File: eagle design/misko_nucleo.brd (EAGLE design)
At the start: 115 x 115 mm, 135 parts, among them IC1 ATMEGA1281-16AU, IC10 ORG1510-MK4, IC11 TPS3808G33DBVT, IC12 LTC4425, IC13 RN4678_BT_MODULE, IC14 ADXL345, IC15 74HCT1G32, IC16 FM25W256-SOIC, IC17 MICROSD_SPI_MODE, IC18 FH12-30S-0.5SH, IC19 DS1394U-33+, IC2 MC1525TT, IC23 SP3012-04UTG, IC3 TMP36GRTZ, IC4 TPS63031, IC5 MCP73871-2AAI/ML, IC6 MAX6818, IC7 FT230XS, IC8 SN74LVC1G3157DBVR - BT switch, IC9 SN74LVC1G3157DBVR - GPS switch, Q1 ABM3B-8MHZ-10-1-U-T, Q2 LFXTAL016178R, SW1 RESET, SW2 POWER SWITCH, SW3 MICROJOYSTICK, SW4 PB6156RSL, SW5 PB6156RSL, T1 BSS84

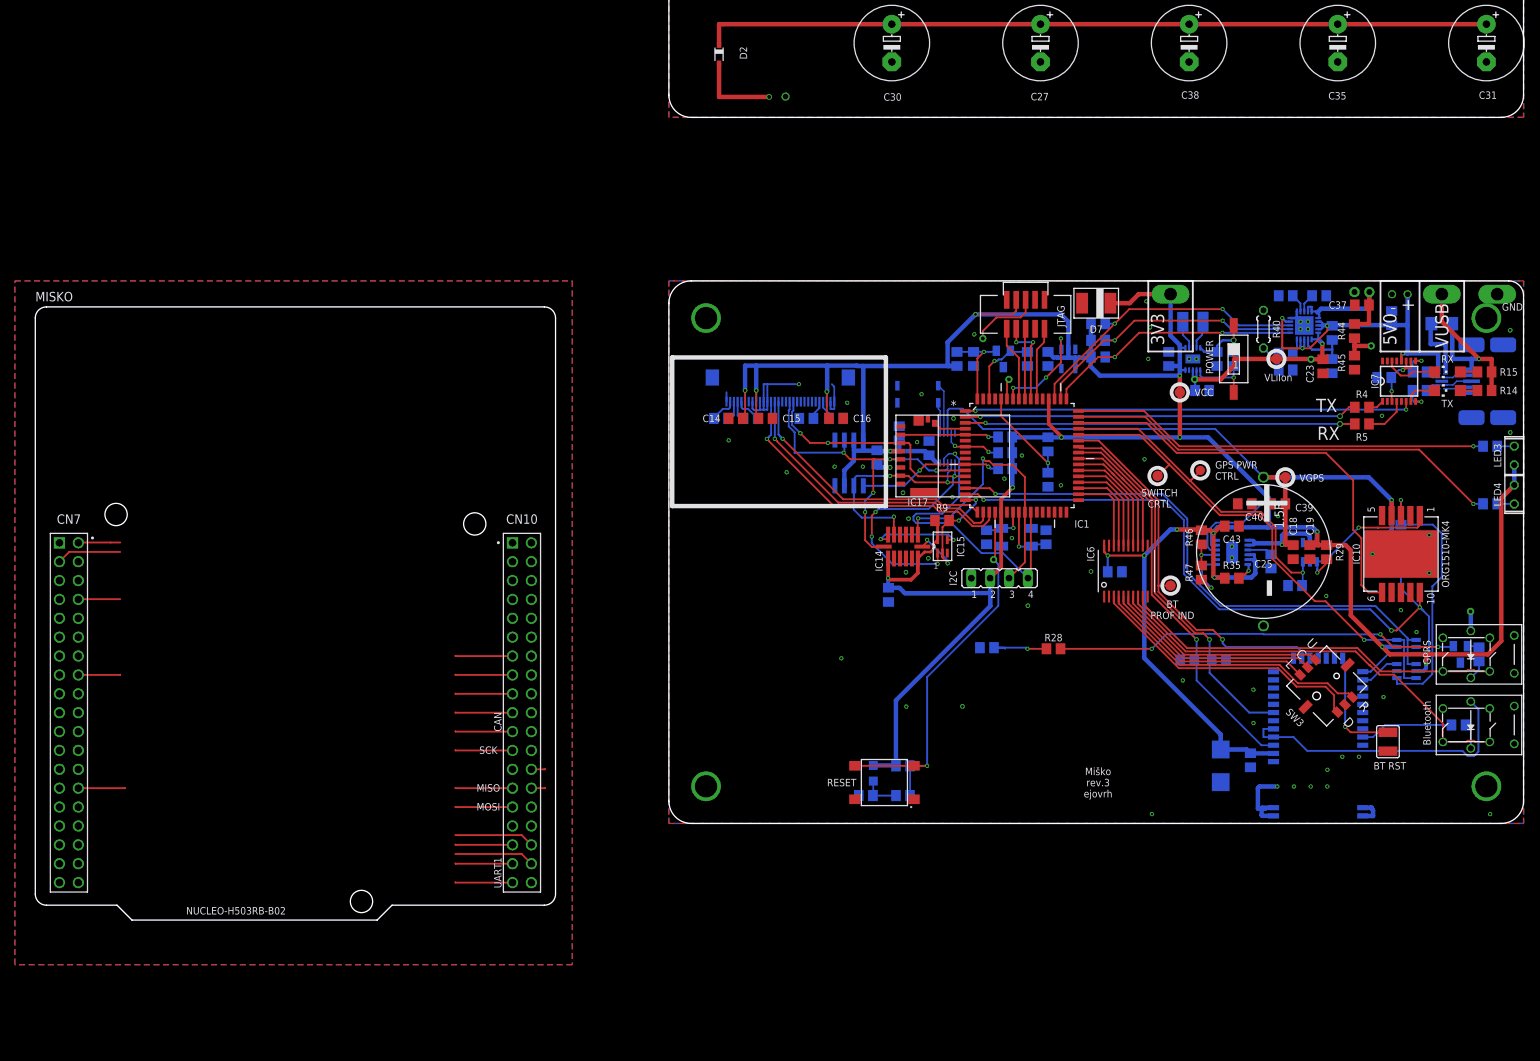
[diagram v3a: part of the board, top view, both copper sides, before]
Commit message: - added ADXL345 module to schematic
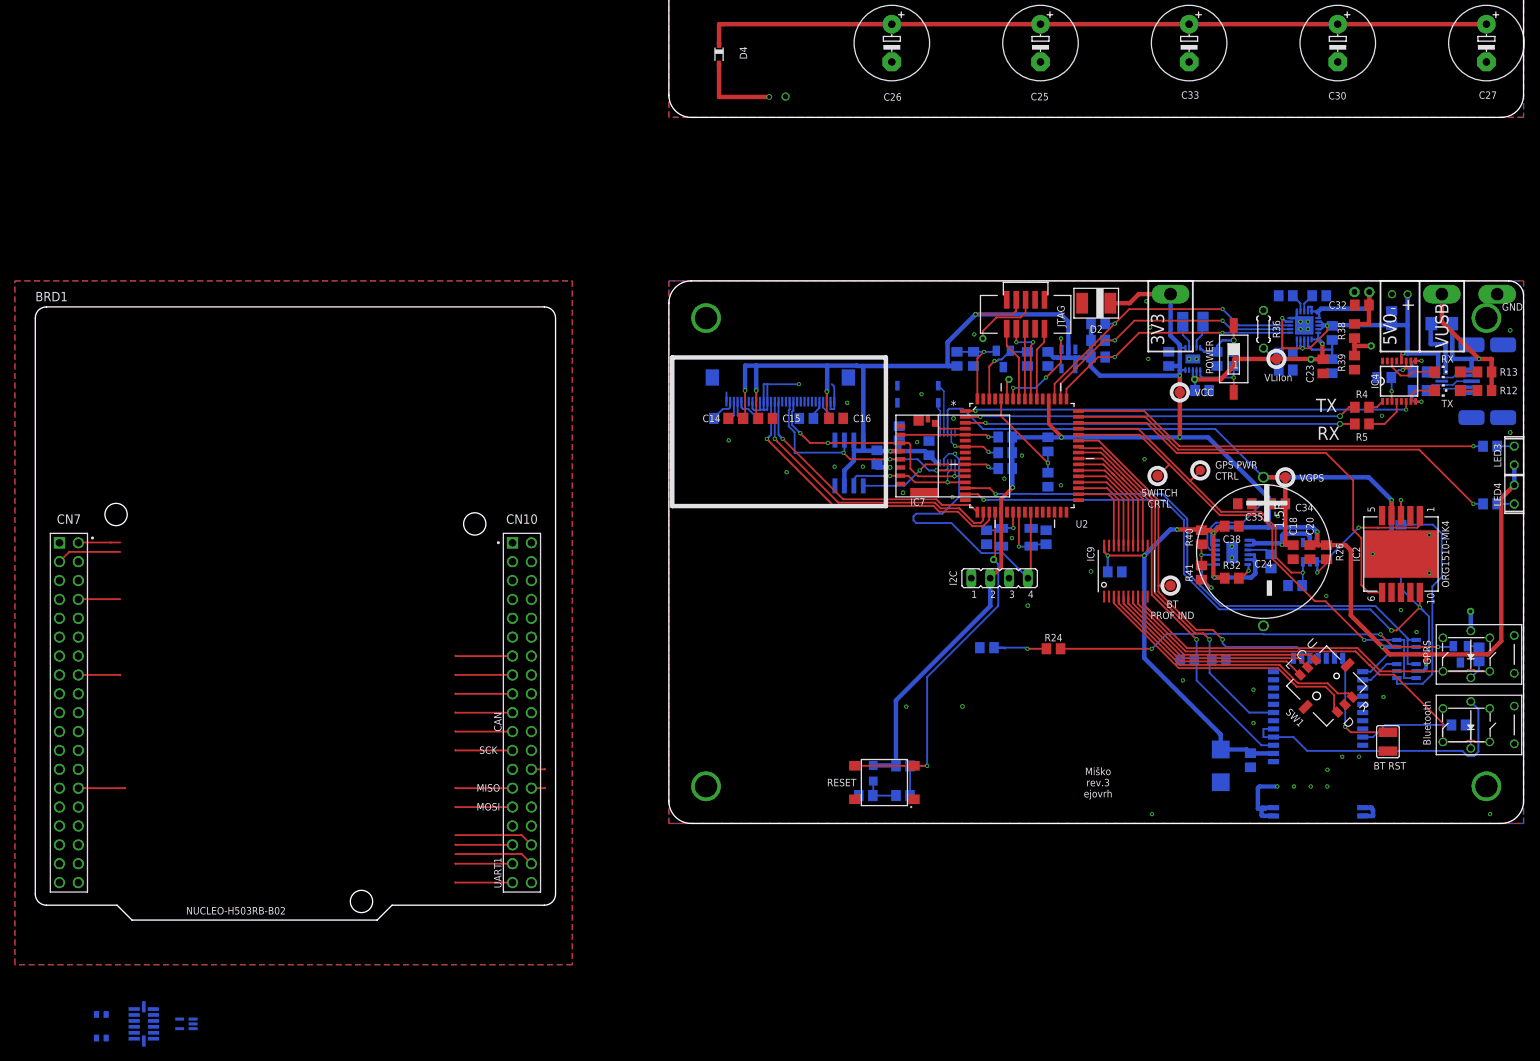
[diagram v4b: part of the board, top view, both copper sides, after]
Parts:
- removed C39, C40: 100µF, rcl:C0805
- removed C41, C42: 0.1µF, resistor:C0805
- removed C43, C45: 0.1µF, rcl:C0805
- removed CONN4: USB mini B, MX-67503-1230 USB Mini-B SMT straight socket:SMT
- removed D7: BZG05C3V6-E3-TR3, zener:DO-214
- removed IC12: LTC4425, LTC4425 Supercap Charger:MSOP
- removed IC13: RN4678_BT_MODULE, RN4678 Bluetooth 4.2 Dual Mode:SMT
- removed IC14: ADXL345, ADXL345 Accelerometer:LGA14
- removed IC15: 74HCT1G32, 74HCT1G32GW:SOT353/5
- removed IC16: FM25W256-SOIC, FM25W256 FERAM:SOIC08
- removed IC17: MICROSD_SPI_MODE, Molex SD-47309 SD Card Slot:MICRO_SD_CONNECTOR
- removed IC19: DS1394U-33+, DS1394U-33+ RTC SPI Module:10UMAX
- removed IC23: SP3012-04UTG, SP3012 TVS Diode Array:μDFN-10
- removed R42, R43: 10k, resistor:R0805
- removed R45: 150k, rcl:R0805
- removed R46, R47: 470k, resistor:R0805
- removed SW4, SW5: PB6156RSL, PB6156RSL Illuminated Tact SPST-NO switch:TH
- removed T1: BSS84, transistor-small-signal:SOT23
- added C104: 0.1u / 16V, rcl:C0402
- added C22, C28: 0.1µF, rcl:C0805
- added C24: 1.5F, EECS5R5H155 Supercap:TH
- added C26, C33: 1000µF, rcl:E5-10,5
- added D3: SZ1SMB5916BT3G, diode:SMB
- added IC101: ADXL345, ADXL345 Accelerometer:LGA14
- added IC102: 74HCT1G32GW, 74HCT1G32GW - OR Gate:SOT353/5
- added JP1: I2C, jumper:JP4
- added Q3: LFXTAL016178R, LFXTAL016178R 32.768kHz crystal:SMD
- added R101: 10k, rcl:R0402
- added R11: 270k, rcl:R0805
- added R21: 47k, rcl:R0805
- added R24: 10k, resistor:R0805
- added R31: 1k, rcl:R0805
- added S1: RESET, Wurth_Elektronik_Electromechanic_Switch_rev17c:430152050836
- added S2: POWER SWITCH, smd-special:SMS-001
- added U1: SN74LVC1G3157DBVR - BT switch, Texas Instruments_By_element14_Batch_1:SOT95P280X145-6N
- added U2: ATMEGA1281-16AU, Atmel_By_element14_Batch_1-00:QFP80P1600X1600X120-64N
- added U3: TPS3808G33DBVT, Texas Instruments_By_element14_Batch_1:SOT95P280X145-6N
- added U4: TMP36GRTZ, TMP36GRTZ:SOT95P280X145-5N
- added U5: MCP73871-2AAI/ML, MCP73871 - Powerpath and Charge Controller:QFN50P400X400X100-21N
- added U6: SN74LVC1G3157DBVR - GPS switch, Texas Instruments_By_element14_Batch_1:SOT95P280X145-6N
- C19: value 0.1µF -> 10µF
- C20, C5: device resistor:C0805 -> rcl:C0805
- C21, C36: device rcl:C0805 -> resistor:C0805
- C25: value 1.5F -> 1000µF; device EECS5R5H155 Supercap:TH -> rcl:E5-10,5
- C31, C38: value 1000µF -> 0.1µF; device rcl:E5-10,5 -> rcl:C0805
- C32, C4: value 0.1µF -> 10µF; device rcl:C0805 -> resistor:C0805
- C34: value 10µF -> 100µF
- C35: value 1000µF -> 100µF; device rcl:E5-10,5 -> rcl:C0805
- C37, C6: value 10µF -> 0.1µF
- CONN1: value JTAG -> USB mini B; device JTAG 1.27mm 10pin header:TH-JTAG -> MX-67503-1230 USB Mini-B SMT straight socket:SMT
- CONN2: value I2C -> JTAG; device jumper:JP4 -> JTAG 1.27mm 10pin header:TH-JTAG
- D2: value BAT60AE6327 -> BZG05C3V6-E3-TR3; device diode:SOD323_ST -> zener:DO-214
- D4: value SZ1SMB5916BT3G -> BAT60AE6327; device diode:SMB -> diode:SOD323_ST
- IC1: value ATMEGA1281-16AU -> MC1525TT; device Atmel_By_element14_Batch_1-00:QFP80P1600X1600X120-64N -> microchip:SOT23
- IC10: value ORG1510-MK4 -> LTC4425; device ORG1510-MK4 GPS module:PACKAGE -> LTC4425 Supercap Charger:MSOP
- IC11: value TPS3808G33DBVT -> SP3012-04UTG; device Texas Instruments_By_element14_Batch_1:SOT95P280X145-6N -> SP3012 TVS Diode Array:μDFN-10
- IC2: value MC1525TT -> ORG1510-MK4; device microchip:SOT23 -> ORG1510-MK4 GPS module:PACKAGE
- IC3: value TMP36GRTZ -> TPS63031; device TMP36GRTZ:SOT95P280X145-5N -> TPS63031 - Buck Boost Voltage Regulator:SMT
- IC4: value TPS63031 -> FT230XS; device TPS63031 - Buck Boost Voltage Regulator:SMT -> ftdichip:SSOP16
- IC5: value MCP73871-2AAI/ML -> RN4678_BT_MODULE; device MCP73871 - Powerpath and Charge Controller:QFN50P400X400X100-21N -> RN4678 Bluetooth 4.2 Dual Mode:SMT
- IC6: value MAX6818 -> FM25W256-SOIC; device MAX6818 CMOS Switch debouncer:TSSOP20 -> FM25W256 FERAM:SOIC08
- IC7: value FT230XS -> MICROSD_SPI_MODE; device ftdichip:SSOP16 -> Molex SD-47309 SD Card Slot:MICRO_SD_CONNECTOR
- IC8: value SN74LVC1G3157DBVR - BT switch -> DS1394U-33+; device Texas Instruments_By_element14_Batch_1:SOT95P280X145-6N -> DS1394U-33+ RTC SPI Module:10UMAX
- IC9: value SN74LVC1G3157DBVR - GPS switch -> MAX6818; device Texas Instruments_By_element14_Batch_1:SOT95P280X145-6N -> MAX6818 CMOS Switch debouncer:TSSOP20
- L1: value DL0805-33 33µH -> DJNR3015-1R5; device rcl:L0805 -> DJNR3015-1R5 Inductor:FFF
- L2: value DJNR3015-1R5 -> DL0805-33 33µH; device DJNR3015-1R5 Inductor:FFF -> rcl:L0805
- Q2: value LFXTAL016178R -> BSS84; device LFXTAL016178R 32.768kHz crystal:SMD -> transistor-small-signal:SOT23
- R10: value 27 -> 100k; device resistor:R0805 -> rcl:R0805
- R12: value 100k -> 1k; device rcl:R0805 -> resistor:R0805
- R13: value 270k -> 1k; device rcl:R0805 -> resistor:R0805
- R14, R18: value 1k -> 10k
- R15: value 1k -> 47k; device resistor:R0805 -> rcl:R0805
- R16: value 47k -> 1k
- R19: value 10k -> 47k
- R20, R25: value 47k -> 1k; device rcl:R0805 -> resistor:R0805
- R22: value 1k -> 390k; device resistor:R0805 -> rcl:R0805
- R26: value 390k -> 1M; device rcl:R0805 -> resistor:R0805
- R29: value 1M -> 10k; device resistor:R0805 -> rcl:R0805
- R30: device resistor:R0805 -> rcl:R0805
- R32: value 10k -> 1k; device rcl:R0805 -> resistor:R0805
- R33: value 1k -> 10k; device rcl:R0805 -> resistor:R0805
- R34: value 1k -> 100k
- R35: value 1k -> 270k; device resistor:R0805 -> rcl:R0805
- R36: value 10k -> NTC 10k; device resistor:R0805 -> rcl:0204/5
- R37: value 100k -> 10k
- R39: value 270k -> 150k
- R40: value NTC 10k -> 470k; device rcl:0204/5 -> resistor:R0805
- R41: value 10k -> 470k; device rcl:R0805 -> resistor:R0805
- R9: value 10k -> 27; device rcl:R0805 -> resistor:R0805
- SW1: value RESET -> MICROJOYSTICK; device Wurth_Elektronik_Electromechanic_Switch_rev17c:430152050836 -> micro joystick:MICROJOYSTICK
- SW2: value POWER SWITCH -> PB6156RSL; device smd-special:SMS-001 -> PB6156RSL Illuminated Tact SPST-NO switch:TH
- SW3: value MICROJOYSTICK -> PB6156RSL; device micro joystick:MICROJOYSTICK -> PB6156RSL Illuminated Tact SPST-NO switch:TH
- moved D4 117.1 mm to (92.0, 116.5), flipped to the top
- moved R22 97.0 mm to (103.8, 67.5)
- moved C31 94.9 mm to (116.2, 65.5), flipped to the bottom, turned to 90 degrees
- moved Q2 81.0 mm to (191.8, 35.8), turned to 180 degrees
- moved C25 74.6 mm to (135.2, 118.0), turned to 270 degrees
- moved R26 72.3 mm to (173.8, 49.5), flipped to the top, turned to 90 degrees
- moved R20 70.9 mm to (191.5, 26.2)
- moved IC7 69.5 mm to (115.8, 56.9)
- moved R25 67.9 mm to (194.2, 35.8), turned to 90 degrees
- moved IC8 67.3 mm to (122.8, 63.5), turned to 270 degrees
- moved R9 67.3 mm to (186.2, 73.8), flipped to the bottom, turned to 180 degrees
- moved R18 65.4 mm to (130.5, 60.8)
- moved C38 65.3 mm to (161.0, 53.0), turned to 180 degrees
- moved C35 63.2 mm to (162.8, 56.0), turned to 0 degrees
- moved C32 61.3 mm to (178.5, 82.8), flipped to the top, turned to 180 degrees
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- renumbered CONN3 to CN1, IC18 to X1, MISKO to BRD1, R44 to R38, SJ3 to SJ1
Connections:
- removed net ADXL345SDA: IC14.SDA, IC15.Y
- removed net ADXL345_INT: BRD1.CN10_17
- new net ADXL345:ADXL345SDA: IC101.SDA, IC102.Y
- new net ADXL345:ADXL345_INT2: IC101.INT2
- new net ADXL345_INT1: BRD1.CN10_17, IC101.INT1
- net 3V3: now also C104.1, IC101.VCC, IC101.VDD, IC102.VCC, R101.2
- net ADXL345_CS: now also IC101.!CS!, IC102.A, R101.1
- net ADXL345_INT1_INTERRUPT_PIN: now also JP1.3, U2.25; no longer CONN2.3, IC1.25, IC14.INT1
- net ANALOG_SW_CTRL_PIN: now also U1.6, U2.44, U6.6; no longer IC1.44, IC8.6, IC9.6
- net AREF: now also C4.1, IC1.2, U2.62; no longer C5.1, IC1.62, IC2.2
- net AVCC: now also C36.2, IC1.1, L2.2, U2.64; no longer C41.2, IC1.64, IC2.1, L1.2
- net BAT_A_PIN: now also R39.1, U2.59; no longer IC1.59, R45.1
- net BLUETOOTH_PROF_IND_PIN: now also IC5.P0_5, U2.43; no longer IC1.43, IC13.P0_5
- net BLUETOOTH_RX: now also IC5.RXD, U1.4; no longer IC13.RXD, IC8.4
- net BLUETOOTH_SWITCH_PIN: now also IC5.SW_BTN, R28.2, U2.41; no longer IC1.41, IC13.SW_BTN, R43.2
- net BLUETOOTH_TX: now also IC5.TXD, U6.3; no longer IC13.TXD, IC9.3
- net BLUETOOTH_WAKEUP_PIN: now also IC5.WAKEUP, R27.2, U2.42; no longer IC1.42, IC13.WAKEUP, R42.2
- net BT_LED: now also IC5.LED, R20.1; no longer IC13.LED, R22.1
- net BUTTON_BLUETOOTH: now also IC9.IN7, SW3.3, SW3.4; no longer IC6.IN7, SW4.3, SW4.4
- net BUTTON_CENTER: now also IC9.IN5, SW1.CENTER; no longer IC6.IN5, SW3.CENTER
- net BUTTON_DOWN: now also IC9.IN2, SW1.DOWN; no longer IC6.IN2, SW3.DOWN
- net BUTTON_GPRS: now also IC9.IN8, SW2.3, SW2.4; no longer IC6.IN8, SW5.3, SW5.4
- net BUTTON_LEFT: now also IC9.IN4, SW1.LEFT; no longer IC6.IN4, SW3.LEFT
- net BUTTON_RIGHT: now also IC9.IN3, SW1.RIGHT; no longer IC6.IN3, SW3.RIGHT
- net BUTTON_UP: now also IC9.IN6, SW1.UP; no longer IC6.IN6, SW3.UP
- net CBUS1: now also IC4.14; no longer IC7.14
- net CBUS2: now also IC4.7; no longer IC7.7
- net D+: now also CONN1.D+, IC11.4; no longer CONN4.D+, IC23.4
- net D-: now also CONN1.D-, IC11.2; no longer CONN4.D-, IC23.2
- net EN: now also IC3.6_EN, S2.1; no longer IC4.6_EN, SW2.1
- net GND: now also C104.2, C19.2, C20.1, C22.2, C24.-, C26.-, C28.2, C31.2, C33.-, C35.1, C36.1, C37.1, C38.1, C5.1, C6.2, CONN1.GND1, CONN1.GND2, CONN1.GND3, CONN1.GND4, CONN1.GND5, CONN2.10_GND, CONN2.2_GND, D2.AN, D3.A, IC1.3, IC101.GND1, IC101.GND2, IC101.GND3, IC102.GND, IC11.3, IC2.GND1, IC2.GND2, IC2.GND3, IC2.GND4, IC2.GND5, IC3.3_PGND, IC3.9_GND1, IC3.GND2, IC3.GND3, IC3.GND4, IC4.13, IC4.5, IC5.GND, IC5.GND1, IC5.GND10, IC5.GND11, IC5.GND12, IC5.GND7, IC5.GND8, IC5.GND9, IC7.GND2, IC7.GND4, IC7.POL, IC7.VSS, IC8.GND, IC9.!EN!, IC9.GND, JP1.1, Q2.3, R11.2, R14.2, R22.1, R27.1, R28.1, R31.2, R33.1, R35.2, R36.2, S1.1, S1.3, SW1.GND1, SW1.GND2, SW1.GND3, SW2.1, SW2.2, SW2.GND1, SW2.GND2, SW3.1, SW3.2, U1.2, U2.22, U2.53, U2.63, U3.2, U4.5, U5.10_GND1, U5.11_GND2, U5.GND2, U5.GND3, U5.GND4, U5.GND5, U5.GND6, U6.2; no longer C19.1, C20.2, C31.-, C34.2, C35.-, C36.2, C37.2, C38.-, C40.1, C41.1, C42.1, C43.1, C45.2, C5.2, C6.1, CONN1.10_GND, CONN1.2_GND, CONN2.1, CONN4.GND1, CONN4.GND2, CONN4.GND3, CONN4.GND4, CONN4.GND5, D4.A, D7.AN, IC1.22, IC1.53, IC1.63, IC10.GND4, IC10.GND5, IC11.2, IC12.GND1, IC12.GND2, IC12.GND3, IC13.GND, IC13.GND1, IC13.GND10, IC13.GND11, IC13.GND12, IC13.GND2, IC13.GND3, IC13.GND4, IC13.GND5, IC13.GND6, IC13.GND7, IC13.GND8, IC13.GND9, IC14.GND1, IC14.GND2, IC14.GND3, IC15.GND, IC16.GND, IC17.GND2, IC17.GND4, IC17.POL, IC17.VSS, IC19.GND, IC2.3, IC23.3, IC3.5, IC4.3_PGND, IC4.9_GND1, IC4.GND2, IC4.GND3, IC4.GND4, IC5.10_GND1, IC5.11_GND2, IC6.!EN!, IC7.13, IC7.5, IC8.2, IC9.2, R13.2, R26.1, R27.2, R36.1, R37.2, R40.2, R42.1, R43.1, R45.2, SW1.1, SW1.3, SW3.GND3, SW4.1, SW4.2, SW4.GND1, SW4.GND2, SW5.1, SW5.2, SW5.GND1, SW5.GND2, T1.3
- net GPRS_NETLIGHT: now also R23.1, R24.1; no longer R27.1, R28.1
- net GPRS_NETLIGHT_GATE: now also Q2.1, R24.2; no longer R28.2, T1.1
- net GPS_GREEN_LED_PIN: now also R16.1, U2.48; no longer IC1.48, R17.1
- net GPS_ON_OFF: now also IC2.ON_OFF, R26.1, U3.1; no longer IC10.ON_OFF, IC11.1, R29.1
- net GPS_POWER_CTL_PIN: now also R14.1, U2.45, U3.3; no longer IC1.45, IC11.3, R23.1
- net GPS_RED_LED_PIN: now also R17.1, U2.47; no longer IC1.47, R18.1
- net GPS_SW_SERIAL_RX: now also U1.1, U2.14, U6.4; no longer IC1.14, IC8.1, IC9.4
- net GPS_SW_SERIAL_TX: now also IC2.RX, U1.3, U2.15; no longer IC1.15, IC10.RX, IC8.3
- net GPS_TX: now also IC2.TX, U6.1; no longer IC10.TX, IC9.1
- net GPS_WAKEUP_PIN: now also IC2.WAKEUP, U2.46; no longer IC1.46, IC10.WAKEUP
- net GREEN_LED: now also R16.2; no longer R17.2
- net ID: now also CONN1.ID, IC11.5; no longer CONN4.ID, IC23.5
- net IREF: now also R22.2; no longer R26.2
- net JTAG_TCL_PIN: now also CONN2.1_JTAG_TCK, U2.57; no longer CONN1.1_JTAG_TCK, IC1.57
- net JTAG_TDI_PIN: now also CONN2.9_JTAG_TDI, U2.54; no longer CONN1.9_JTAG_TDI, IC1.54
- net JTAG_TDO_PIN: now also CONN2.3_JTAG_TDO, U2.55; no longer CONN1.3_JTAG_TDO, IC1.55
- net JTAG_TMS_PIN: now also CONN2.5_JTAG_TMS, U2.56; no longer CONN1.5_JTAG_TMS, IC1.56
- net L2: now also R20.2, SW3.L2; no longer R22.2, SW4.L2
- net LDO18_O: now also IC5.LDO18_O; no longer IC13.LDO18_O
- net LDO33_O: now also IC5.LDO33_O, IC5.VDD_IO, SW3.L1; no longer IC13.LDO33_O, IC13.VDD_IO, SW4.L1
- net LTC4425_EN: now also IC10.EN, R32.2; no longer IC12.EN, R35.2
- net LTC4425_PROG: now also IC10.PROG, R33.2; no longer IC12.PROG, R36.2
- net L_L1: now also IC3.4_L1, L1.P$1; no longer IC4.4_L1, L2.P$1
- net L_L2: now also IC3.2_L2, L1.P$2; no longer IC4.2_L2, L2.P$2
- net MCP73871_CHARGE_STATUS_1_PIN: now also R21.2, U2.51, U5.8_STAT1; no longer IC1.51, IC5.8_STAT1, R25.2
- net MCP73871_CHARGE_STATUS_2_PIN: now also R19.2, U2.50, U5.7_STAT2; no longer IC1.50, IC5.7_STAT2, R20.2
- net MCP73871_POWER_GOOD_PIN: now also R15.2, U2.49, U5.!6_PG!; no longer IC1.49, IC5.!6_PG!, R16.2
- net MENU_BLUETOOTH_POWER_BUTTON_PIN: now also IC9.OUT7, U2.39; no longer IC1.39, IC6.OUT7
- net MENU_CENTER_BUTTON_PIN: now also IC9.OUT5, U2.37; no longer IC1.37, IC6.OUT5
- net MENU_DOWN_BUTTON_PIN: now also IC9.OUT2, U2.34; no longer IC1.34, IC6.OUT2
- net MENU_GPRS_POWER_BUTTON_PIN: now also IC9.OUT8, U2.40; no longer IC1.40, IC6.OUT8
- net MENU_LEFT_BUTTON_PIN: now also IC9.OUT4, U2.36; no longer IC1.36, IC6.OUT4
- net MENU_RIGHT_BUTTON_PIN: now also IC9.OUT3, U2.35; no longer IC1.35, IC6.OUT3
- net MENU_UP_BUTTON_PIN: now also IC9.OUT6, U2.38; no longer IC1.38, IC6.OUT6
- net N$1: now also R25.1, SW2.L2; no longer R30.1, SW5.L2
- net N$10: now also IC4.10, IC4.11, IC4.3; no longer IC7.10, IC7.11, IC7.3
- net N$11: now also IC5.!RST_N!; no longer IC13.!RST_N!
- net N$19: now also R30.2, R35.1, R36.1; no longer R33.2, R39.1, R40.1
- net N$3: now also Q2.2, R25.2; no longer R30.2, T1.2
- net N$4: now also IC11.1; no longer IC23.1
- net N$6: now also C25.+, C26.+, C33.+, D4.C; no longer C31.+, C35.+, C38.+, D2.C
- net OLD_5V0: now also C37.2, D4.A, IC11.10, IC4.12, R10.1, U5.17_CE, U5.18_IN1, U5.19_IN2, U5.3_SEL, U5.4_PROG2, U5.9_!TE!; no longer C42.2, D2.A, IC23.10, IC5.17_CE, IC5.18_IN1, IC5.19_IN2, IC5.3_SEL, IC5.4_PROG2, IC5.9_!TE!, IC7.12, R12.1
- net PDI_UART0_CTS_PIN: now also IC4.6, U2.1; no longer IC1.1, IC7.6
- net PDI_UART0_RX_PIN: now also U2.2; no longer IC1.2
- net PDI_UART0_TX_PIN: now also U2.3; no longer IC1.3
- net PFI: now also IC10.PFI, R40.1, R41.2; no longer IC12.PFI, R46.1, R47.2
- net PFI_RET: now also IC10.PFI_RET, R41.1; no longer IC12.PFI_RET, R47.1
- net PROG1: now also R31.1, U5.13_PROG1; no longer IC5.13_PROG1, R34.1
- net PROG3: now also R34.1, U5.12_PROG3; no longer IC5.12_PROG3, R37.1
- net RED_LED: now also R17.2; no longer R18.2
- net RESET: now also CONN2.6_JTAG_RST, S1.2, S1.4, U2.20; no longer CONN1.6_JTAG_RST, IC1.20, SW1.2, SW1.4
- net RTC_INT_INTERRUPT_PIN: now also IC8.!INT!, JP1.4, U2.26; no longer CONN2.4, IC1.26, IC19.!INT!
- net RTC_XTAL1: now also IC8.X1, Q3.XTAL1; no longer IC19.X1, Q2.XTAL1
- net RTC_XTAL2: now also IC8.X2, Q3.XTAL2; no longer IC19.X2, Q2.XTAL2
- net RXD: now also IC4.4; no longer IC7.4
- net SD_CARD_DETECT_PIN: now also IC7.DET, U2.4; no longer IC1.4, IC17.DET
- net SPI1_MISO: now also IC101.SDO
- net SPI1_MOSI: now also IC102.B
- net SPI1_SCK: now also IC101.SCL
- net SPI_MISO_PIN: now also IC6.SO, IC7.DAT0, IC8.DOUT, U2.13; no longer IC1.13, IC14.SDO, IC16.SO, IC17.DAT0, IC19.DOUT
- net SPI_MOSI_PIN: now also IC6.SI, IC7.CMD, IC8.DIN, U2.12; no longer IC1.12, IC15.B, IC16.SI, IC17.CMD, IC19.DIN
- net SPI_OLED_D/C_PIN: now also U2.17; no longer IC1.17
- net SPI_OLED_RESET_PIN: now also U2.18; no longer IC1.18
- net SPI_SCK_PIN: now also IC6.SCK, IC7.CLK, IC8.SCLK, U2.11; no longer IC1.11, IC14.SCL, IC16.SCK, IC17.CLK, IC19.SCLK
- net SPI_SS_ADXL345_PIN: now also U2.16; no longer IC1.16, IC14.!CS!, IC15.A, R9.2
- net SPI_SS_FRAM_PIN: now also IC6.!CS!, R18.1, U2.10; no longer IC1.10, IC16.!CS!, R19.1
- net SPI_SS_OLED_PIN: now also U2.19; no longer IC1.19
- net SPI_SS_RTC_PIN: now also IC8.!CS!, R29.2, U2.7; no longer IC1.7, IC19.!CS!, R32.2
- net SPI_SS_SD_CARD_PIN: now also IC7.CD/DAT3, R37.1, U2.5; no longer IC1.5, IC17.CD/DAT3, R41.1
- net THERM: now also R30.1, U5.5_THERM; no longer IC5.5_THERM, R33.1
- net TMP36_VSENSE_PIN: now also U2.58, U4.1; no longer IC1.58, IC3.1
- net TXD: now also IC4.1; no longer IC7.1
- net UART1_GPS_RX: now also U2.27; no longer IC1.27
- net UART1_GPS_TX: now also U2.28; no longer IC1.28
- net USBDM: now also IC4.9, R9.1; no longer IC7.9, R10.1
- net USBDP: now also IC4.8; no longer IC7.8
- net USB_D+: now also IC11.7; no longer IC23.7
- net USB_D-: now also IC11.9, R9.2; no longer IC23.9, R10.2
- net USB_ID: now also IC11.6; no longer IC23.6
- net USB_RX_LED: now also R12.2; no longer R14.2
- net USB_TX_LED: now also R13.2; no longer R15.2
- net VCC: now also C19.1, C20.2, C22.1, C28.1, C31.1, C38.2, CONN2.4_VCC, D2.CAT, D3.C, IC10.FB, IC10.SEL, IC10.VIN1, IC10.VIN2, IC3.10_FB, IC3.1_VOUT, IC5.BAT_IN, IC6.!HOLD!, IC6.!WP!, IC7.VDD, IC8.VCC, IC9.VCC, JP1.2, L2.1, R15.1, R18.2, R19.1, R21.1, R26.2, R29.1, R37.2, R40.2, U1.5, U2.21, U2.52, U3.6, U4.2, U4.4, U6.5; no longer C19.2, C20.1, C32.1, C34.1, C36.1, C4.1, C43.2, CONN1.4_VCC, CONN2.2, D4.C, D7.CAT, IC1.21, IC1.52, IC11.6, IC12.FB, IC12.SEL, IC12.VIN1, IC12.VIN2, IC13.BAT_IN, IC14.VCC, IC14.VDD, IC15.VCC, IC16.!HOLD!, IC16.!WP!, IC16.VCC, IC17.VDD, IC19.VCC, IC3.2, IC3.4, IC4.10_FB, IC4.1_VOUT, IC8.5, IC9.5, L1.1, R16.1, R19.2, R20.1, R25.1, R29.2, R35.1, R41.2, R46.2, R9.1
- net VCC_SENSE_PIN: now also U2.60; no longer IC1.60
- net VGPS: now also C24.+, C34.1, IC10.VOUT1, IC10.VOUT2, IC2.VCC, IC8.VBACK, U3.5; no longer C25.+, C39.1, IC10.VCC, IC11.5, IC12.VOUT1, IC12.VOUT2, IC19.VBACK
- net VMID: now also C34.2, C35.2, IC10.VMID; no longer C39.2, C40.2, IC12.VMID
- net VPCC: now also R10.2, R11.1, U5.2_VPCC; no longer IC5.2_VPCC, R12.2, R13.1
- net VUSB: now also CONN1.VBUS, R12.1, R13.1; no longer CONN4.VBUS, R14.1, R15.1
- net V_LIION+: now also C32.1, U5.14_VBAT1, U5.15_VBAT2, U5.16_BAT_SENSE; no longer C37.1, IC5.14_VBAT1, IC5.15_VBAT2, IC5.16_BAT_SENSE
- net V_LIION_REGULATED: now also C5.2, C6.1, IC3.5_VIN, IC3.7_PS/SYNC, IC3.8_VINA, S2.2, SW2.L1, U5.1_OUT1, U5.20_OUT2; no longer C45.1, C6.2, IC4.5_VIN, IC4.7_PS/SYNC, IC4.8_VINA, IC5.1_OUT1, IC5.20_OUT2, SW2.2, SW5.L1
- net XTAL1: now also U2.24; no longer IC1.24
- net XTAL2: now also U2.23; no longer IC1.23
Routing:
- net ADXL345_INT1_INTERRUPT_PIN: track 37.5 -> 0.00 mm, vias 2 -> 0
- net VCC: track 479.7 -> 448.3 mm, vias 18 -> 17
- net SPI_MOSI_PIN: track 63.4 -> 34.3 mm, vias 6 -> 3
- net SPI_SS_ADXL345_PIN: track 18.3 -> 0.00 mm, vias 4 -> 0
- net SPI_SCK_PIN: track 51.2 -> 36.9 mm, vias 5 -> 3
- net SPI_MISO_PIN: track 32.2 -> 19.3 mm, vias 3 -> 2
- net ADXL345SDA: track 12.8 -> 0.00 mm, vias 2 -> 0
- net ADXL345_INT1: track 0.00 -> 7.71 mm
- net ADXL345_INT: track 7.71 -> 0.00 mm
- net GND: vias 48 -> 44
